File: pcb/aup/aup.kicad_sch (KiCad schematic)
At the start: 0 parts

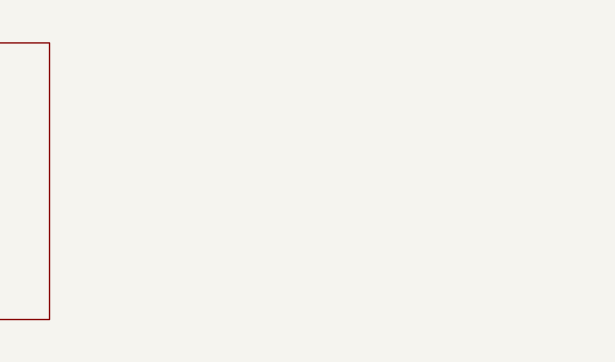
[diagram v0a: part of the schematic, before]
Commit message: Add 5v regulator to external power portion
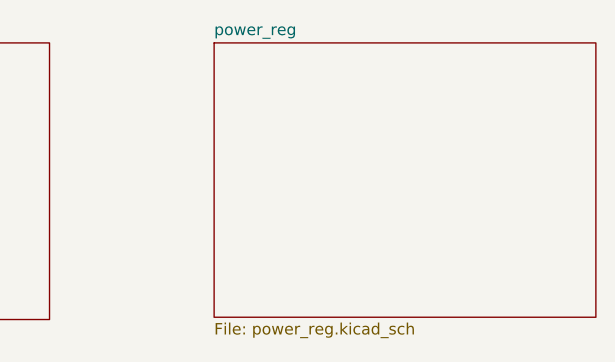
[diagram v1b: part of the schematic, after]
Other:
- added sheet power_reg (power_reg.kicad_sch)
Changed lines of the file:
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@@
 	(paper "USLetter")
+	(sheet
+		(at 92.964 40.64)
+		(size 42.418 30.48)
+		(exclude_from_sim no)
+		(in_bom yes)
+		(on_board yes)
+		(dnp no)
+		(fields_autoplaced yes)
+		(stroke
+			(width 0.1524)
+			(type solid)
+		)
+		(fill
+			(color 0 0 0 0.0000)
+		)
+		(property "Sheetname" "power_reg"
+			(at 92.964 39.9284 0)
+			(effects
+				(font
+					(size 1.27 1.27)
+				)
+				(justify left bottom)
+			)
+		)
+		(property "Sheetfile" "power_reg.kicad_sch"
+			(at 92.964 71.7046 0)
+			(effects
+				(font
+					(size 1.27 1.27)
+				)
+				(justify left top)
+			)
+		)
+		(instances
+			(project "aup"
+				(path "/312a869c-f247-4883-8e23-bdad51e1754f"
+					(page "3")
+				)
+			)
+		)
+	)
 	(sheet
 		(at 30.48 40.64)

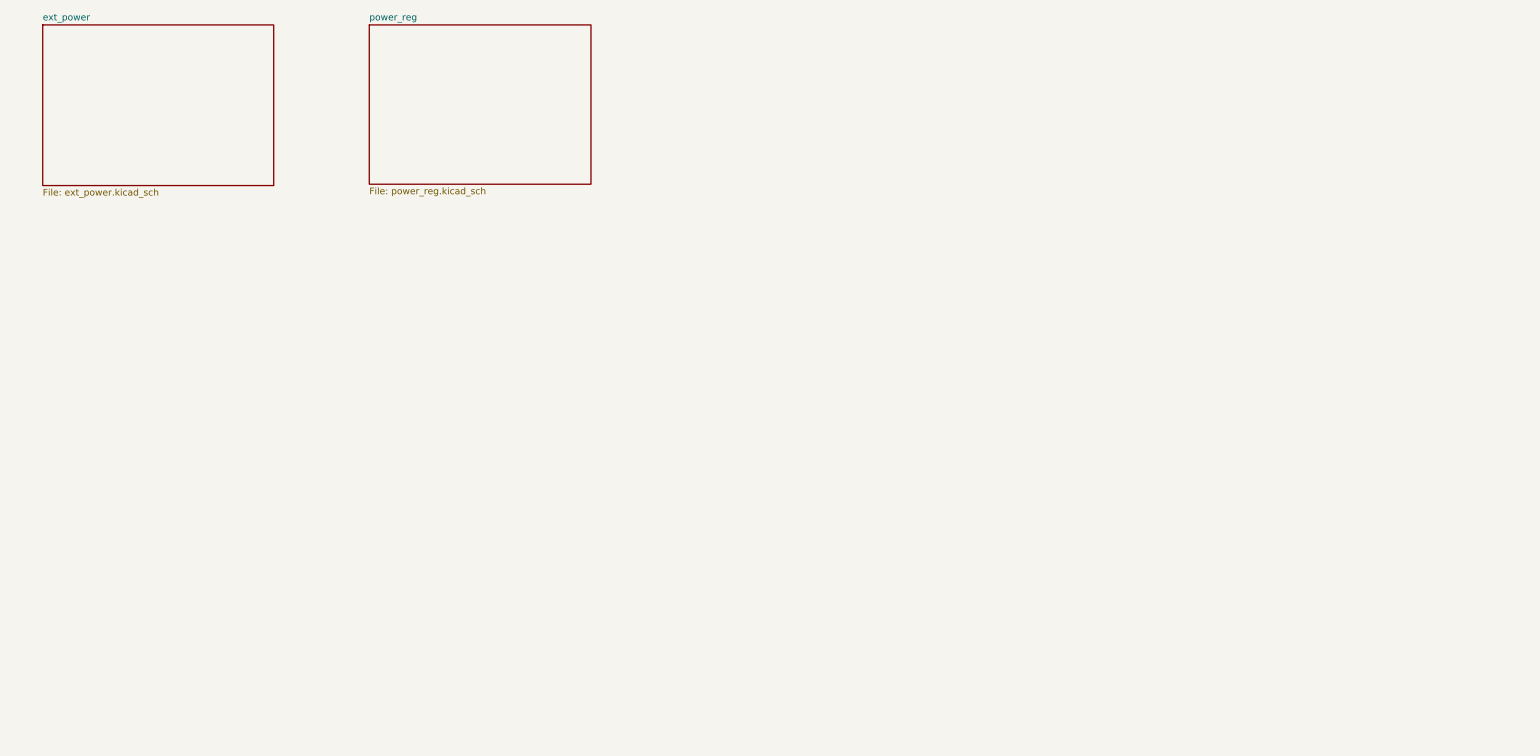
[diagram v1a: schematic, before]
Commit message: Added symbols for the major components
It should be possible to do a first pass placement of ICs on the pcb as
a rough fit check.

Most imported footprints are still missing models.
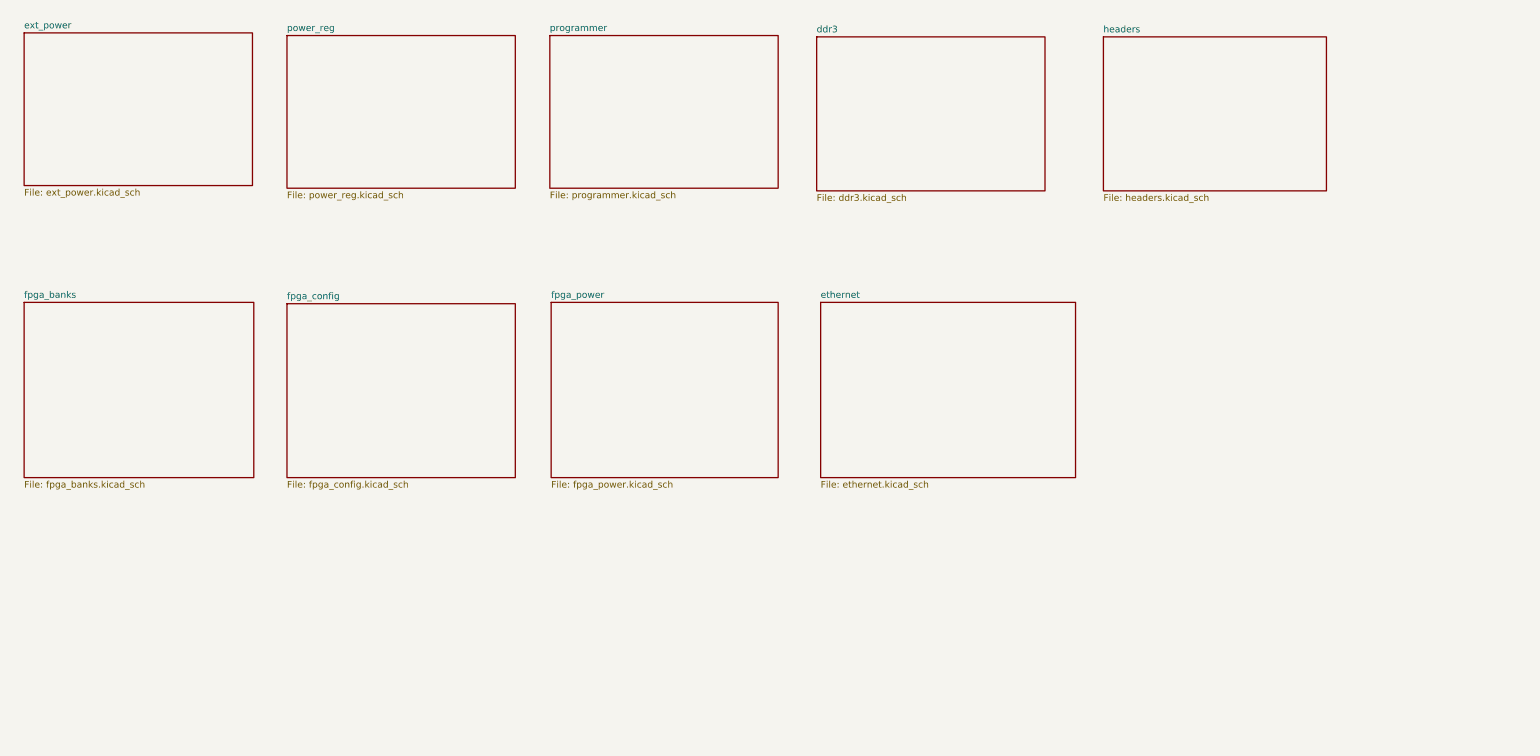
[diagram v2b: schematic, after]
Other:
- added sheet ddr3 (ddr3.kicad_sch)
- added sheet ethernet (ethernet.kicad_sch)
- added sheet fpga_banks (fpga_banks.kicad_sch)
- added sheet fpga_config (fpga_config.kicad_sch)
- added sheet fpga_power (fpga_power.kicad_sch)
- added sheet headers (headers.kicad_sch)
- added sheet programmer (programmer.kicad_sch)

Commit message: Misc updates - too hard to see in a diff after a delay
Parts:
- added U4: ADP5054, Package_DFN_QFN:QFN-48-1EP_7x7mm_P0.5mm_EP5.15x5.15mm, symbol Regulator_Switching:ADP5054
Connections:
- new net: U4.10 (PGND4), U4.11 (PGND4)
- new net: U4.2 (PGND3), U4.3 (PGND3)
- new net: U4.22 (PVIN2), U4.23 (PVIN2), U4.24 (PVIN2)
- new net: U4.25 (SW2), U4.26 (SW2), U4.27 (SW2)
- new net: U4.33 (SW1), U4.34 (SW1), U4.35 (SW1)
- new net: U4.36 (PVIN1), U4.37 (PVIN1), U4.38 (PVIN1)
- new net: U4.4 (SW3), U4.5 (SW3)
- new net: U4.8 (SW4), U4.9 (SW4)
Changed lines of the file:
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@@
 	(generator_version "9.0")
 	(paper "USLedger")
+	(symbol
+		(lib_id "Regulator_Switching:ADP5054")
+		(at 287.02 118.11 0)
+		(unit 1)
+		(exclude_from_sim no)
+		(in_bom yes)
+		(on_board yes)
+		(dnp no)
+		(fields_autoplaced yes)
+		(property "Reference" "U4"
+			(at 287.02 90.17 0)
+			(effects
+				(font
+					(size 1.27 1.27)
+				)
+			)
+		)
+		(property "Value" "ADP5054"
+			(at 287.02 92.71 0)
+			(effects
+				(font
+					(size 1.27 1.27)
+				)
+			)
+		)
+		(property "Footprint" "Package_DFN_QFN:QFN-48-1EP_7x7mm_P0.5mm_EP5.15x5.15mm"
+			(at 320.04 162.56 0)
+			(effects
+				(font
+					(size 1.27 1.27)
+				)
+				(hide yes)
+			)
+		)
+		(property "Datasheet" "https://www.analog.com/media/en/technical-documentation/data-sheets/ADP5054.pdf"
+			(at 259.08 100.33 0)
+			(effects
+				(font
+					(size 1.27 1.27)
+				)
+				(hide yes)
+			)
+		)
+		(property "Description" "250kHz to 2MHz, 6A/6A/2A/2A Quad Buck Regulator, -40 to +125C, QFN-48"
+			(at 287.02 118.11 0)
+			(effects
+				(font
+					(size 1.27 1.27)
+				)
+				(hide yes)
+			)
+		)
+		(pin "34"
+		)
+		(pin "15"
+		)
+		(pin "19"
+		)
+		(pin "33"
+		)
+		(pin "24"
+		)
+		(pin "14"
+		)
+		(pin "31"
+		)
+		(pin "1"
+		)
+		(pin "17"
+		)
+		(pin "40"
+		)
+		(pin "48"
+		)
+		(pin "22"
+		)
+		(pin "21"
+		)
+		(pin "35"
+		)
+		(pin "41"
+		)
+		(pin "25"
+		)
+		(pin "16"
+		)
+		(pin "20"
+		)
+		(pin "32"
+		)
+		(pin "13"
+		)
+		(pin "27"
+		)
+		(pin "26"
+		)
+		(pin "44"
+		)
+		(pin "10"
+		)
+		(pin "49"
+		)
+		(pin "8"
+		)
+		(pin "4"
+		)
+		(pin "12"
+		)
+		(pin "9"
+		)
+		(pin "5"
+		)
+		(pin "46"
+		)
+		(pin "28"
+		)
+		(pin "11"
+		)
+		(pin "39"
+		)
+		(pin "38"
+		)
+		(pin "3"
+		)
+		(pin "2"
+		)
+		(pin "23"
+		)
+		(pin "42"
+		)
+		(pin "7"
+		)
+		(pin "45"
+		)
+		(pin "43"
+		)
+		(pin "36"
+		)
+		(pin "37"
+		)
+		(pin "29"
+		)
+		(pin "6"
+		)
+		(pin "47"
+		)
+		(pin "18"
+		)
+		(pin "30"
+		)
+		(instances
+			(project ""
+				(path "/312a869c-f247-4883-8e23-bdad51e1754f"
+					(reference "U4")
+					(unit 1)
+				)
+			)
+		)
+	)
 	(sheet
 		(at 77.216 42.672)

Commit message: More upsized planning
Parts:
- removed U4: ADP5054, Package_DFN_QFN:QFN-48-1EP_7x7mm_P0.5mm_EP5.15x5.15mm, symbol Regulator_Switching:ADP5054
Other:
- removed sheet ethernet
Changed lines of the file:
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@@
 	(generator_version "9.0")
 	(paper "USLedger")
-	(symbol
-		(lib_id "Regulator_Switching:ADP5054")
-		(at 287.02 118.11 0)
-		(unit 1)
-		(exclude_from_sim no)
-		(in_bom yes)
-		(on_board yes)
-		(dnp no)
-		(fields_autoplaced yes)
-		(property "Reference" "U4"
-			(at 287.02 90.17 0)
-			(effects
-				(font
-					(size 1.27 1.27)
-				)
-			)
-		)
-		(property "Value" "ADP5054"
-			(at 287.02 92.71 0)
-			(effects
-				(font
-					(size 1.27 1.27)
-				)
-			)
-		)
-		(property "Footprint" "Package_DFN_QFN:QFN-48-1EP_7x7mm_P0.5mm_EP5.15x5.15mm"
-			(at 320.04 162.56 0)
-			(effects
-				(font
-					(size 1.27 1.27)
-				)
-				(hide yes)
-			)
-		)
-		(property "Datasheet" "https://www.analog.com/media/en/technical-documentation/data-sheets/ADP5054.pdf"
-			(at 259.08 100.33 0)
-			(effects
-				(font
-					(size 1.27 1.27)
-				)
-				(hide yes)
-			)
-		)
-		(property "Description" "250kHz to 2MHz, 6A/6A/2A/2A Quad Buck Regulator, -40 to +125C, QFN-48"
-			(at 287.02 118.11 0)
-			(effects
-				(font
-					(size 1.27 1.27)
-				)
-				(hide yes)
-			)
-		)
-		(pin "34"
-		)
-		(pin "15"
-		)
-		(pin "19"
-		)
-		(pin "33"
-		)
-		(pin "24"
-		)
-		(pin "14"
-		)
-		(pin "31"
-		)
-		(pin "1"
-		)
-		(pin "17"
-		)
-		(pin "40"
-		)
-		(pin "48"
-		)
-		(pin "22"
-		)
-		(pin "21"
-		)
-		(pin "35"
-		)
-		(pin "41"
-		)
-		(pin "25"
-		)
-		(pin "16"
-		)
-		(pin "20"
-		)
-		(pin "32"
-		)
-		(pin "13"
-		)
-		(pin "27"
-		)
-		(pin "26"
-		)
-		(pin "44"
-		)
-		(pin "10"
-		)
-		(pin "49"
-		)
-		(pin "8"
-		)
-		(pin "4"
-		)
-		(pin "12"
-		)
-		(pin "9"
-		)
-		(pin "5"
-		)
-		(pin "46"
-		)
-		(pin "28"
-		)
-		(pin "11"
-		)
-		(pin "39"
-		)
-		(pin "38"
-		)
-		(pin "3"
-		)
-		(pin "2"
-		)
-		(pin "23"
-		)
-		(pin "42"
-		)
-		(pin "7"
-		)
-		(pin "45"
-		)
-		(pin "43"
-		)
-		(pin "36"
-		)
-		(pin "37"
-		)
-		(pin "29"
-		)
-		(pin "6"
-		)
-		(pin "47"
-		)
-		(pin "18"
-		)
-		(pin "30"
-		)
-		(instances
-			(project ""
-				(path "/312a869c-f247-4883-8e23-bdad51e1754f"
-					(reference "U4")
-					(unit 1)
-				)
-			)
-		)
-	)
 	(sheet
 		(at 77.216 42.672)
@@
 				)
 			)
-		)
-	)
-	(sheet
-		(at 179.324 93.726)
-		(size 48.768 33.528)
-		(exclude_from_sim no)
-		(in_bom yes)
-		(on_board yes)
-		(dnp no)
-		(fields_autoplaced yes)
-		(stroke
-			(width 0.1524)
-			(type solid)
-		)
-		(fill
-			(color 0 0 0 0.0000)
-		)
-		(property "Sheetname" "ethernet"
-			(at 179.324 93.0144 0)
-			(effects
-				(font
-					(size 1.27 1.27)
-				)
-				(justify left bottom)
-			)
-		)
-		(property "Sheetfile" "ethernet.kicad_sch"
-			(at 179.324 127.8386 0)
-			(effects
-				(font
-					(size 1.27 1.27)
-				)
-				(justify left top)
-			)
-		)
-		(instances
-			(project "aup"
-				(path "/312a869c-f247-4883-8e23-bdad51e1754f"
-					(page "10")
-				)
-			)

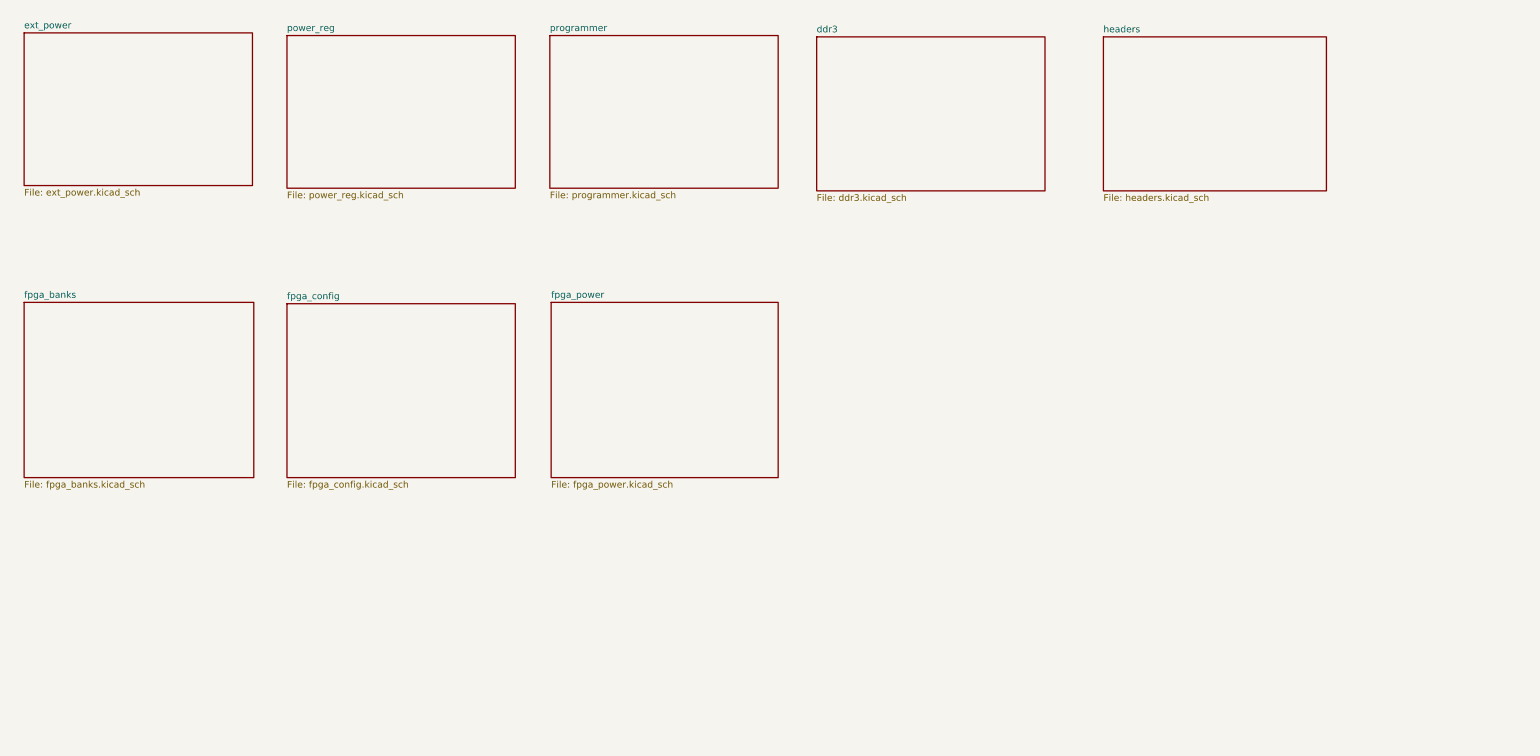
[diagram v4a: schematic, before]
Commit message: Add hierarchical sheets for banks and add caps.
There are some stale sheets in this commit, but I don't want to delete
an active one accidentally. Save them all for now, and then go back and
clean them up.
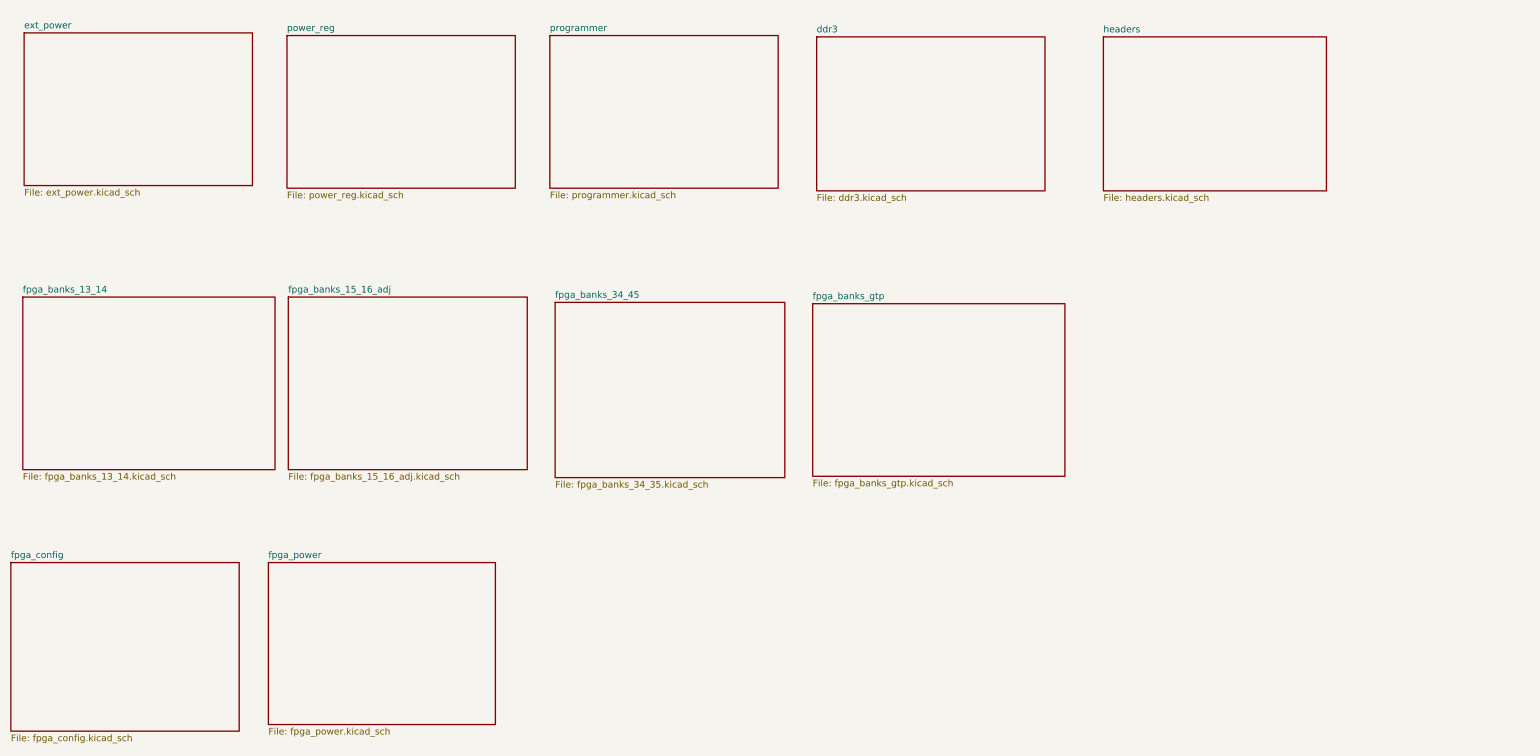
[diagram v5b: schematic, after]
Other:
- sheet fpga_banks renamed fpga_banks_34_45
- added sheet fpga_banks_13_14 (fpga_banks_13_14.kicad_sch)
- added sheet fpga_banks_15_16_adj (fpga_banks_15_16_adj.kicad_sch)
- added sheet fpga_banks_gtp (fpga_banks_gtp.kicad_sch)
- sheet fpga_banks_34_45: file fpga_banks.kicad_sch -> fpga_banks_34_35.kicad_sch
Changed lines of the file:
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@@
 	)
 	(sheet
-		(at 26.924 93.726)
+		(at 128.524 93.726)
 		(size 43.942 33.528)
 		(exclude_from_sim no)
@@
 			(color 0 0 0 0.0000)
 		)
-		(property "Sheetname" "fpga_banks"
-			(at 26.924 93.0144 0)
-			(effects
-				(font
-					(size 1.27 1.27)
-				)
-				(justify left bottom)
-			)
-		)
-		(property "Sheetfile" "fpga_banks.kicad_sch"
-			(at 26.924 127.8386 0)
+		(property "Sheetname" "fpga_banks_34_45"
+			(at 128.524 93.0144 0)
+			(effects
+				(font
+					(size 1.27 1.27)
+				)
+				(justify left bottom)
+			)
+		)
+		(property "Sheetfile" "fpga_banks_34_35.kicad_sch"
+			(at 128.524 127.8386 0)
 			(effects
 				(font
@@
 				(path "/312a869c-f247-4883-8e23-bdad51e1754f"
 					(page "7")
+				)
+			)
+		)
+	)
+	(sheet
+		(at 77.47 92.71)
+		(size 45.72 33.02)
+		(exclude_from_sim no)
+		(in_bom yes)
+		(on_board yes)
+		(dnp no)
+		(fields_autoplaced yes)
+		(stroke
+			(width 0.1524)
+			(type solid)
+		)
+		(fill
+			(color 0 0 0 0.0000)
+		)
+		(property "Sheetname" "fpga_banks_15_16_adj"
+			(at 77.47 91.9984 0)
+			(effects
+				(font
+					(size 1.27 1.27)
+				)
+				(justify left bottom)
+			)
+		)
+		(property "Sheetfile" "fpga_banks_15_16_adj.kicad_sch"
+			(at 77.47 126.3146 0)
+			(effects
+				(font
+					(size 1.27 1.27)
+				)
+				(justify left top)
+			)
+		)
+		(instances
+			(project "aup"
+				(path "/312a869c-f247-4883-8e23-bdad51e1754f"
+					(page "11")
 				)
 			)
@@
 	)
 	(sheet
-		(at 127.762 93.726)
-		(size 43.434 33.528)
+		(at 26.67 92.71)
+		(size 48.26 33.02)
+		(exclude_from_sim no)
+		(in_bom yes)
+		(on_board yes)
+		(dnp no)
+		(fields_autoplaced yes)
+		(stroke
+			(width 0.1524)
+			(type solid)
+		)
+		(fill
+			(color 0 0 0 0.0000)
+		)
+		(property "Sheetname" "fpga_banks_13_14"
+			(at 26.67 91.9984 0)
+			(effects
+				(font
+					(size 1.27 1.27)
+				)
+				(justify left bottom)
+			)
+		)
+		(property "Sheetfile" "fpga_banks_13_14.kicad_sch"
+			(at 26.67 126.3146 0)
+			(effects
+				(font
+					(size 1.27 1.27)
+				)
+				(justify left top)
+			)
+		)
+		(instances
+			(project "aup"
+				(path "/312a869c-f247-4883-8e23-bdad51e1754f"
+					(page "12")
+				)
+			)
+		)
+	)
+	(sheet
+		(at 73.66 143.51)
+		(size 43.434 30.988)
 		(exclude_from_sim no)
 		(in_bom yes)
@@
 		)
 		(property "Sheetname" "fpga_power"
-			(at 127.762 93.0144 0)
+			(at 73.66 142.7984 0)
 			(effects
 				(font
@@
 		)
 		(property "Sheetfile" "fpga_power.kicad_sch"
-			(at 127.762 127.8386 0)
+			(at 73.66 175.0826 0)
 			(effects
 				(font
@@
 	)
 	(sheet
+		(at 177.8 93.98)
+		(size 48.26 33.02)
+		(exclude_from_sim no)
+		(in_bom yes)
+		(on_board yes)
+		(dnp no)
+		(fields_autoplaced yes)
+		(stroke
+			(width 0.1524)
+			(type solid)
+		)
+		(fill
+			(color 0 0 0 0.0000)
+		)
+		(property "Sheetname" "fpga_banks_gtp"
+			(at 177.8 93.2684 0)
+			(effects
+				(font
+					(size 1.27 1.27)
+				)
+				(justify left bottom)
+			)
+		)
+		(property "Sheetfile" "fpga_banks_gtp.kicad_sch"
+			(at 177.8 127.5846 0)
+			(effects
+				(font
+					(size 1.27 1.27)
+				)
+				(justify left top)
+			)
+		)
+		(instances
+			(project "aup"
+				(path "/312a869c-f247-4883-8e23-bdad51e1754f"
+					(page "11")
+				)
+			)
+		)
+	)
+	(sheet
 		(at 233.426 42.926)
 		(size 42.672 29.464)
@@
 	)
 	(sheet
-		(at 77.216 93.98)
-		(size 43.688 33.274)
+		(at 24.384 143.51)
+		(size 43.688 32.258)
 		(exclude_from_sim no)
 		(in_bom yes)
@@
 		)
 		(property "Sheetname" "fpga_config"
-			(at 77.216 93.2684 0)
+			(at 24.384 142.7984 0)
 			(effects
 				(font
@@
 		)
 		(property "Sheetfile" "fpga_config.kicad_sch"
-			(at 77.216 127.8386 0)
-			(effects
-				(font
+			(at 24.384 176.3526 0)
+			(effects
+				(font
